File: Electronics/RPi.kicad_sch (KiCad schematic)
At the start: 3 parts, among them J5 Raspberry_Pi_2_3

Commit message: made some changes
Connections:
- net PiServo2: now reaches J5.22 (GPIO25)
- net PiServo1: now reaches J5.24 (~{CE0}/GPIO8)
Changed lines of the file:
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@@
+    (stroke (width 0) (type default) (color 0 0 0 0))
+  )
+  (wire (pts (xy 121.92 97.79) (xy 127 97.79))
     (stroke (width 0) (type default) (color 0 0 0 0))
   )
@@
     (stroke (width 0) (type default) (color 0 0 0 0))
   )
+  (wire (pts (xy 167.64 90.17) (xy 173.99 90.17))
+    (stroke (width 0) (type default) (color 0 0 0 0))
+  )
   (hierarchical_label "RPi Power" (shape input) (at 60.96 45.72 180)
     (effects (font (size 1.27 1.27)) (justify right))
@@
   )
   (hierarchical_label "Reset ESP" (shape output) (at 121.92 95.25 180)
+    (effects (font (size 1.27 1.27)) (justify right))
+  )
+  (hierarchical_label "PiServo2" (shape output) (at 121.92 97.79 180)
     (effects (font (size 1.27 1.27)) (justify right))
   )
@@
     (effects (font (size 1.27 1.27)) (justify right))
   )
+  (hierarchical_label "PiServo1" (shape output) (at 173.99 90.17 0)
+    (effects (font (size 1.27 1.27)) (justify left))
+  )
   (hierarchical_label "Keep Alive" (shape output) (at 184.15 77.47 0)

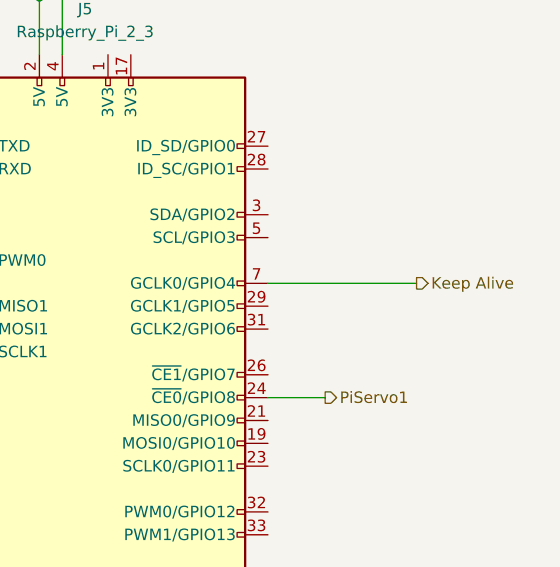
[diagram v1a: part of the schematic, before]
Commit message: added bom
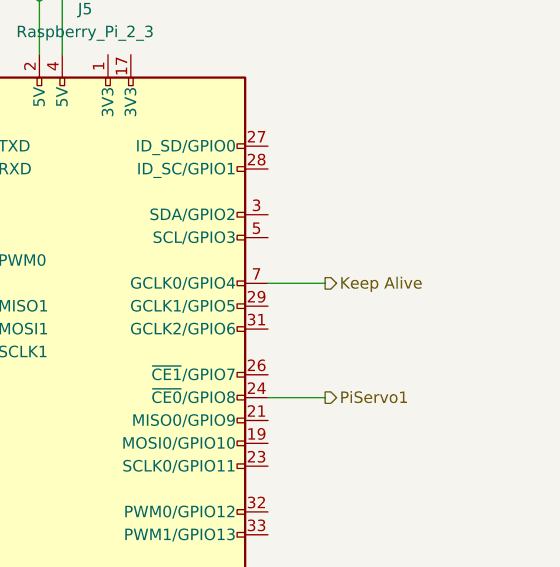
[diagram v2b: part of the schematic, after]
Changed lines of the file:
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@@
     (stroke (width 0) (type default) (color 0 0 0 0))
   )
-  (wire (pts (xy 167.64 77.47) (xy 184.15 77.47))
+  (wire (pts (xy 167.64 77.47) (xy 173.99 77.47))
     (stroke (width 0) (type default) (color 0 0 0 0))
   )
@@
     (effects (font (size 1.27 1.27)) (justify right))
   )
+  (hierarchical_label "Keep Alive" (shape output) (at 173.99 77.47 0)
+    (effects (font (size 1.27 1.27)) (justify left))
+  )
   (hierarchical_label "PiServo1" (shape output) (at 173.99 90.17 0)
     (effects (font (size 1.27 1.27)) (justify left))
   )
-  (hierarchical_label "Keep Alive" (shape output) (at 184.15 77.47 0)
-    (effects (font (size 1.27 1.27)) (justify left))
-  )

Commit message: del backups
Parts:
- renumbered C25 to C27, C26 to C28, J5 to J6
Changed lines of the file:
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@@
   (symbol (lib_id "power:GND") (at 63.5 68.58 0) (unit 1)
     (in_bom yes) (on_board yes)
-    (property "Reference" "#PWR068" (id 0) (at 63.5 74.93 0)
+    (property "Reference" "#PWR059" (id 0) (at 63.5 74.93 0)
       (effects (font (size 1.27 1.27)) hide)
     )
@@
   (symbol (lib_id "power:GND") (at 76.2 68.58 0) (unit 1)
     (in_bom yes) (on_board yes)
-    (property "Reference" "#PWR069" (id 0) (at 76.2 74.93 0)
+    (property "Reference" "#PWR060" (id 0) (at 76.2 74.93 0)
       (effects (font (size 1.27 1.27)) hide)
     )
@@
   (symbol (lib_id "power:GND") (at 137.16 123.19 0) (unit 1)
     (in_bom yes) (on_board yes) (fields_autoplaced)
-    (property "Reference" "#PWR070" (id 0) (at 137.16 129.54 0)
+    (property "Reference" "#PWR061" (id 0) (at 137.16 129.54 0)
       (effects (font (size 1.27 1.27)) hide)
     )
@@
   (symbol (lib_id "Device:C_Small") (at 63.5 62.23 0) (unit 1)
     (in_bom yes) (on_board yes) (fields_autoplaced)
-    (property "Reference" "C25" (id 0) (at 66.04 60.9599 0)
+    (property "Reference" "C27" (id 0) (at 66.04 60.9599 0)
       (effects (font (size 1.27 1.27)) (justify left))
     )
@@
   (symbol (lib_id "Device:C_Small") (at 76.2 62.23 0) (unit 1)
     (in_bom yes) (on_board yes) (fields_autoplaced)
-    (property "Reference" "C26" (id 0) (at 78.74 60.9599 0)
+    (property "Reference" "C28" (id 0) (at 78.74 60.9599 0)
       (effects (font (size 1.27 1.27)) (justify left))
     )
@@
   (symbol (lib_id "Connector:Raspberry_Pi_2_3") (at 147.32 85.09 0) (unit 1)
     (in_bom yes) (on_board yes) (fields_autoplaced)
-    (property "Reference" "J5" (id 0) (at 147.32 46.99 0))
+    (property "Reference" "J6" (id 0) (at 147.32 46.99 0))
     (property "Value" "Raspberry_Pi_2_3" (id 1) (at 147.32 49.53 0))
     (property "Footprint" "Connector_PinHeader_2.54mm:PinHeader_2x20_P2.54mm_Vertical" (id 2) (at 147.32 85.09 0)

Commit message: yep
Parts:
- renumbered C27 to C28, C28 to C29
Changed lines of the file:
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@@
   (symbol (lib_id "power:GND") (at 63.5 68.58 0) (unit 1)
     (in_bom yes) (on_board yes)
-    (property "Reference" "#PWR059" (id 0) (at 63.5 74.93 0)
+    (property "Reference" "#PWR060" (id 0) (at 63.5 74.93 0)
       (effects (font (size 1.27 1.27)) hide)
     )
@@
   (symbol (lib_id "power:GND") (at 76.2 68.58 0) (unit 1)
     (in_bom yes) (on_board yes)
-    (property "Reference" "#PWR060" (id 0) (at 76.2 74.93 0)
+    (property "Reference" "#PWR061" (id 0) (at 76.2 74.93 0)
       (effects (font (size 1.27 1.27)) hide)
     )
@@
   (symbol (lib_id "power:GND") (at 137.16 123.19 0) (unit 1)
     (in_bom yes) (on_board yes) (fields_autoplaced)
-    (property "Reference" "#PWR061" (id 0) (at 137.16 129.54 0)
+    (property "Reference" "#PWR062" (id 0) (at 137.16 129.54 0)
       (effects (font (size 1.27 1.27)) hide)
     )
@@
   (symbol (lib_id "Device:C_Small") (at 63.5 62.23 0) (unit 1)
     (in_bom yes) (on_board yes) (fields_autoplaced)
-    (property "Reference" "C27" (id 0) (at 66.04 60.9599 0)
+    (property "Reference" "C28" (id 0) (at 66.04 60.9599 0)
       (effects (font (size 1.27 1.27)) (justify left))
     )
@@
   (symbol (lib_id "Device:C_Small") (at 76.2 62.23 0) (unit 1)
     (in_bom yes) (on_board yes) (fields_autoplaced)
-    (property "Reference" "C28" (id 0) (at 78.74 60.9599 0)
+    (property "Reference" "C29" (id 0) (at 78.74 60.9599 0)
       (effects (font (size 1.27 1.27)) (justify left))
     )

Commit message: some changes were made
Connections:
- net GND: no longer J6.9 (GND)
- net Program: now also J6.13 (GPIO27); no longer J6.16 (GPIO23)
- net Reset ESP: now also J6.11 (GPIO17); no longer J6.18 (GPIO24)
- no-connect marks 0 -> 1
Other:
- company: Philip McGaw -> Squashed Fly

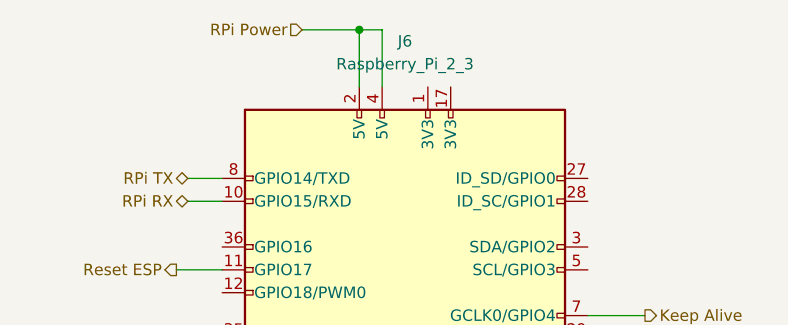
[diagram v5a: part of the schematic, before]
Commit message: removed the backups
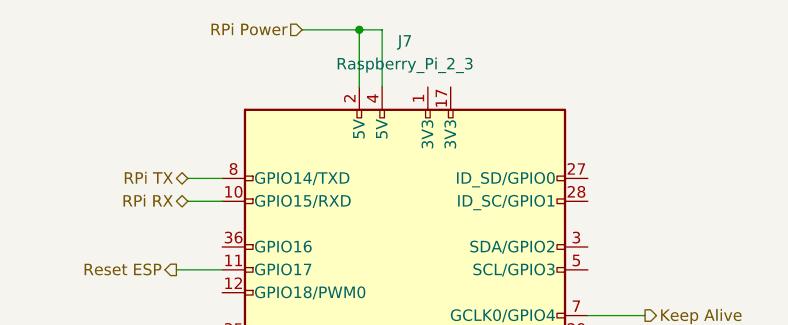
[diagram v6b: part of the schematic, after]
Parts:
- renumbered J6 to J7
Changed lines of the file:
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@@
   (junction (at 152.4 120.65) (diameter 0) (color 0 0 0 0))
   (junction (at 144.78 120.65) (diameter 0) (color 0 0 0 0))
+  (junction (at 142.24 45.72) (diameter 0) (color 0 0 0 0))
+  (junction (at 142.24 120.65) (diameter 0) (color 0 0 0 0))
+  (junction (at 137.16 120.65) (diameter 0) (color 0 0 0 0))
+  (junction (at 149.86 120.65) (diameter 0) (color 0 0 0 0))
+  (junction (at 147.32 120.65) (diameter 0) (color 0 0 0 0))
   (junction (at 63.5 45.72) (diameter 0) (color 0 0 0 0))
-  (junction (at 147.32 120.65) (diameter 0) (color 0 0 0 0))
-  (junction (at 137.16 120.65) (diameter 0) (color 0 0 0 0))
-  (junction (at 142.24 120.65) (diameter 0) (color 0 0 0 0))
-  (junction (at 142.24 45.72) (diameter 0) (color 0 0 0 0))
-  (junction (at 149.86 120.65) (diameter 0) (color 0 0 0 0))
   (no_connect (at 139.7 118.11))
   (wire (pts (xy 123.19 64.77) (xy 127 64.77))
@@
   (symbol (lib_id "power:GND") (at 63.5 68.58 0) (unit 1)
     (in_bom yes) (on_board yes)
-    (property "Reference" "#PWR072" (id 0) (at 63.5 74.93 0)
+    (property "Reference" "#PWR070" (id 0) (at 63.5 74.93 0)
       (effects (font (size 1.27 1.27)) hide)
     )
@@
   (symbol (lib_id "Connector:Raspberry_Pi_2_3") (at 147.32 85.09 0) (unit 1)
     (in_bom yes) (on_board yes) (fields_autoplaced)
-    (property "Reference" "J6" (id 0) (at 147.32 46.99 0))
+    (property "Reference" "J7" (id 0) (at 147.32 46.99 0))
     (property "Value" "Raspberry_Pi_2_3" (id 1) (at 147.32 49.53 0))
     (property "Footprint" "Connector_PinHeader_2.54mm:PinHeader_2x20_P2.54mm_Vertical" (id 2) (at 147.32 85.09 0)
@@
   (symbol (lib_id "power:GND") (at 137.16 123.19 0) (unit 1)
     (in_bom yes) (on_board yes) (fields_autoplaced)
-    (property "Reference" "#PWR074" (id 0) (at 137.16 129.54 0)
+    (property "Reference" "#PWR072" (id 0) (at 137.16 129.54 0)
       (effects (font (size 1.27 1.27)) hide)
     )
@@
   (symbol (lib_id "power:GND") (at 76.2 68.58 0) (unit 1)
     (in_bom yes) (on_board yes)
-    (property "Reference" "#PWR073" (id 0) (at 76.2 74.93 0)
-      (effects (font (size 1.27 1.27)) hide)
-    )
+    (property "Reference" "#PWR071" (id 0) (at 76.2 74.93 0)
+      (effects (font (size 1.27 1.27)) hide)
+    )
